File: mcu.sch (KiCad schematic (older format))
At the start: 13 parts, among them J3 jtag conector, U4 STM32F103C8Tx, U5 STM32F031K6Ux

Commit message: duży update, gotowe pcb
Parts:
- removed R16: 10R, Resistor_SMD:R_0603_1608Metric, symbol Device:R
- removed U5: STM32F031K6Ux, Package_DFN_QFN:QFN-32-1EP_5x5mm_P0.5mm_EP3.45x3.45mm, symbol MCU_ST_STM32F0:STM32F031K6Ux
- added C20: 100n, Capacitor_SMD:C_0603_1608Metric_Pad1.05x0.95mm_HandSolder, symbol Device:C
- added J4: Conn_01x04_Female, Connector_PinHeader_2.54mm:PinHeader_1x04_P2.54mm_Vertical, symbol Connector:Conn_01x04_Female
- R14: footprint (none) -> Resistor_SMD:R_0603_1608Metric_Pad1.05x0.95mm_HandSolder
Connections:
- net labels added: scl, sda
- wire segments 78 -> 69
- no-connect marks 0 -> 28
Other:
- note removed: "STM32F030C8Tx pasuje wystrczy zrobć nc na 36 i 35 \nfootprint się zgadza tylko \npin 36 to VDD\npin35 to GND\n\n"

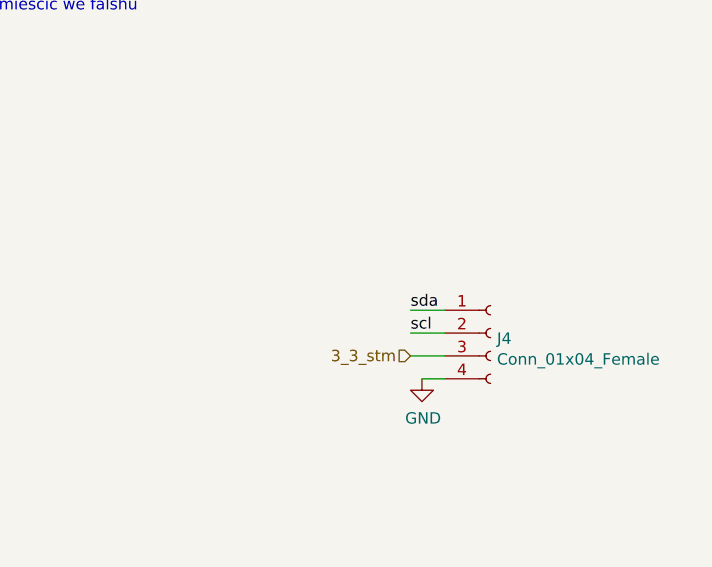
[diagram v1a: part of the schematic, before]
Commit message: dodanie pullup do i2c i screenow
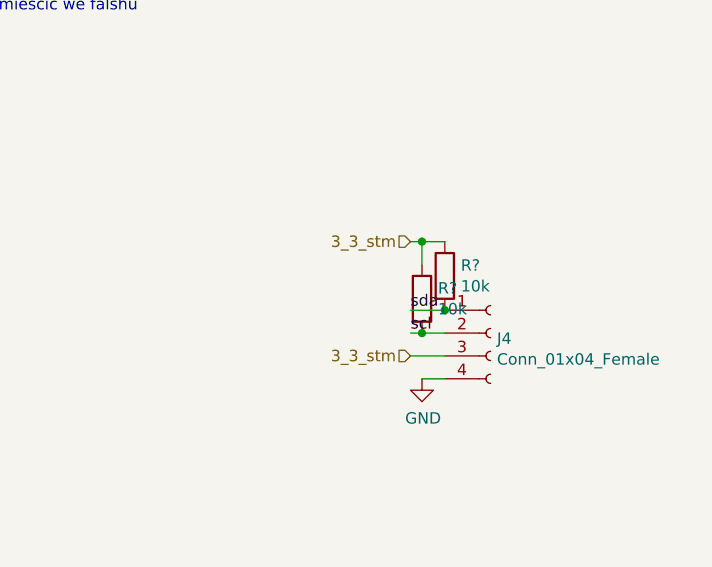
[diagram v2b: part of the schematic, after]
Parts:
- added R? (x2): 10k, Resistor_SMD:R_0603_1608Metric, symbol Device:R
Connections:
- wire segments 69 -> 73
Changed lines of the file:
@@
 	8050 3500 8200 3500
 Wire Wire Line
-	8200 3400 8050 3400
+	8200 3400 8100 3400
 Wire Wire Line
 	8200 3300 8050 3300
@@
 Wire Wire Line
 	4700 1700 4700 1600
+$Comp
+L Device:R R?
+U 1 1 5CEC68D2
+P 8200 3150
+F 0 "R?" H 8270 3196 50  0000 L CNN
+F 1 "10k" H 8270 3105 50  0000 L CNN
+F 2 "Resistor_SMD:R_0603_1608Metric" V 8130 3150 50  0001 C CNN
+F 3 "~" H 8200 3150 50  0001 C CNN
+	1    8200 3150
+	1    0    0    -1
+$EndComp
+Connection ~ 8200 3300
+$Comp
+L Device:R R?
+U 1 1 5CEC6FCF
+P 8100 3250
+F 0 "R?" H 8170 3296 50  0000 L CNN
+F 1 "10k" H 8170 3205 50  0000 L CNN
+F 2 "Resistor_SMD:R_0603_1608Metric" V 8030 3250 50  0001 C CNN
+F 3 "~" H 8100 3250 50  0001 C CNN
+	1    8100 3250
+	1    0    0    -1
+$EndComp
+Connection ~ 8100 3400
+Wire Wire Line
+	8100 3400 8050 3400
+Text HLabel 8050 3000 0    50   Input ~ 0
+3_3_stm
+Wire Wire Line
+	8050 3000 8100 3000
+Wire Wire Line
+	8100 3000 8100 3100
+Wire Wire Line
+	8100 3000 8200 3000
+Connection ~ 8100 3000
 $EndSCHEMATC

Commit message: poprawki na sch
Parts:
- removed J3: jtag conector, Connector_PinHeader_1.27mm:PinHeader_2x04_P1.27mm_Vertical_SMD, symbol Connector_Generic_MountingPin:Conn_01x10_MountingPin
- added J3: Conn_02x04_Odd_Even, Connector_PinHeader_1.27mm:PinHeader_2x04_P1.27mm_Vertical_SMD, symbol Connector_Generic:Conn_02x04_Odd_Even
- gave numbers to parts that had none: 2
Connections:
- wire segments 73 -> 76
- no-connect marks 28 -> 25
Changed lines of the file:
@@
 EESchema Schematic File Version 4
 LIBS:WELLER-cache
-EELAYER 29 0
+EELAYER 26 0
 EELAYER END
 $Descr A4 11693 8268
@@
 Wire Wire Line
 	2500 2250 2500 2650
-$Comp
-L Connector_Generic_MountingPin:Conn_01x10_MountingPin J3
-U 1 1 5CB74020
-P 2250 4800
-F 0 "J3" H 2337 4622 50  0000 L CNN
-F 1 "jtag conector" H 2337 4713 50  0000 L CNN
-F 2 "Connector_PinHeader_1.27mm:PinHeader_2x04_P1.27mm_Vertical_SMD" H 2250 4800 50  0001 C CNN
-F 3 "~" H 2250 4800 50  0001 C CNN
-	1    2250 4800
-	-1   0    0    1
-$EndComp
 Text Notes 5700 2000 0    50   ~ 0
 można by dodać eeprom do zapisaywania danych dot temp ?\n->powinno się zmieścić we falshu\n
@@
 Wire Wire Line
 	4400 5900 4500 5900
-Text Label 2650 4300 0    50   ~ 0
+Text Label 1600 4200 0    50   ~ 0
 nRST
-Wire Wire Line
-	2450 4300 2650 4300
-Wire Wire Line
-	2450 5100 2800 5100
-Wire Wire Line
-	2450 4900 2800 4900
-Text Label 2800 5100 0    50   ~ 0
+Text Label 1600 4400 0    50   ~ 0
 SWDIO
-Text Label 2800 4900 0    50   ~ 0
+Text Label 1600 4300 0    50   ~ 0
 SWCLK
 Connection ~ 4800 2350
 Wire Wire Line
 	4800 2350 4800 2500
-Text Label 2800 5200 0    50   ~ 0
+Text Label 1600 4500 0    50   ~ 0
 3_3v
-Wire Wire Line
-	2800 5200 2450 5200
-$Comp
-L power:GND #PWR0132
-U 1 1 5CC8470F
-P 2600 5000
-F 0 "#PWR0132" H 2600 4750 50  0001 C CNN
-F 1 "GND" H 2605 4827 50  0000 C CNN
-F 2 "" H 2600 5000 50  0001 C CNN
-F 3 "" H 2600 5000 50  0001 C CNN
-	1    2600 5000
-	0    -1   -1   0
-$EndComp
-Wire Wire Line
-	2600 5000 2450 5000
-$Comp
-L power:GND #PWR0133
-U 1 1 5CC87D51
-P 2600 4800
-F 0 "#PWR0133" H 2600 4550 50  0001 C CNN
-F 1 "GND" H 2605 4627 50  0000 C CNN
-F 2 "" H 2600 4800 50  0001 C CNN
-F 3 "" H 2600 4800 50  0001 C CNN
-	1    2600 4800
-	0    -1   -1   0
-$EndComp
-Wire Wire Line
-	2600 4800 2450 4800
 $Comp
 L power:GND #PWR0134
 U 1 1 5CC89512
-P 2600 4600
-F 0 "#PWR0134" H 2600 4350 50  0001 C CNN
-F 1 "GND" H 2605 4427 50  0000 C CNN
-F 2 "" H 2600 4600 50  0001 C CNN
-F 3 "" H 2600 4600 50  0001 C CNN
-	1    2600 4600
-	0    -1   -1   0
-$EndComp
-Wire Wire Line
-	2600 4600 2450 4600
-$Comp
-L power:GND #PWR0135
-U 1 1 5CC8BC59
-P 2600 4400
-F 0 "#PWR0135" H 2600 4150 50  0001 C CNN
-F 1 "GND" H 2605 4227 50  0000 C CNN
-F 2 "" H 2600 4400 50  0001 C CNN
-F 3 "" H 2600 4400 50  0001 C CNN
-	1    2600 4400
-	0    -1   -1   0
-$EndComp
-Wire Wire Line
-	2600 4400 2450 4400
+P 900 4300
+F 0 "#PWR0134" H 900 4050 50  0001 C CNN
+F 1 "GND" H 905 4127 50  0000 C CNN
+F 2 "" H 900 4300 50  0001 C CNN
+F 3 "" H 900 4300 50  0001 C CNN
+	1    900  4300
+	0    1    1    0
+$EndComp
 Wire Wire Line
 	4600 2050 4600 2600
@@
 NoConn ~ 3900 5300
 NoConn ~ 3900 5400
-NoConn ~ 2450 4500
-NoConn ~ 2450 4700
-NoConn ~ 2250 4100
 $Comp
 L power:PWR_FLAG #FLG0101
@@
 	4700 1700 4700 1600
 $Comp
-L Device:R R?
+L Device:R R17
 U 1 1 5CEC68D2
 P 8200 3150
-F 0 "R?" H 8270 3196 50  0000 L CNN
+F 0 "R17" H 8270 3196 50  0000 L CNN
 F 1 "10k" H 8270 3105 50  0000 L CNN
 F 2 "Resistor_SMD:R_0603_1608Metric" V 8130 3150 50  0001 C CNN
@@
 Connection ~ 8200 3300
 $Comp
-L Device:R R?
+L Device:R R16
 U 1 1 5CEC6FCF
 P 8100 3250
-F 0 "R?" H 8170 3296 50  0000 L CNN
+F 0 "R16" H 8170 3296 50  0000 L CNN
 F 1 "10k" H 8170 3205 50  0000 L CNN
 F 2 "Resistor_SMD:R_0603_1608Metric" V 8030 3250 50  0001 C CNN
@@
 	8100 3000 8200 3000
 Connection ~ 8100 3000
+$Comp
+L Connector_Generic:Conn_02x04_Odd_Even J3
+U 1 1 5CEE64F6
+P 1200 4300
+F 0 "J3" H 1250 4617 50  0000 C CNN
+F 1 "Conn_02x04_Odd_Even" H 1250 4526 50  0000 C CNN
+F 2 "Connector_PinHeader_1.27mm:PinHeader_2x04_P1.27mm_Vertical_SMD" H 1200 4300 50  0001 C CNN
+F 3 "~" H 1200 4300 50  0001 C CNN
+	1    1200 4300
+	1    0    0    -1
+$EndComp
+Wire Wire Line
+	1000 4200 900  4200
+Wire Wire Line
+	900  4200 900  4300
+Wire Wire Line
+	900  4300 900  4400
+Wire Wire Line
+	900  4500 1000 4500
+Connection ~ 900  4300
+Wire Wire Line
+	1000 4400 900  4400
+Connection ~ 900  4400
+Wire Wire Line
+	900  4400 900  4500
+Wire Wire Line
+	900  4300 1000 4300
+Wire Wire Line
+	1500 4200 1600 4200
+Wire Wire Line
+	1600 4300 1500 4300
+Wire Wire Line
+	1500 4400 1600 4400
+Wire Wire Line
+	1600 4500 1500 4500
 $EndSCHEMATC

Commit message: duży update, drc przechodzi
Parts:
- added R18: 560k, Resistor_SMD:R_0603_1608Metric, symbol Device:R
- added R19: 100k, Resistor_SMD:R_0603_1608Metric, symbol Device:R
- added U5: SM353LT, Package_TO_SOT_SMD:SOT-23, symbol Sensor_Magnetic:SM353LT
- J3: value Conn_02x04_Odd_Even -> debug+programing; footprint Connector_PinHeader_1.27mm:PinHeader_2x04_P1.27mm_Vertical_SMD -> Connector_PinHeader_1.27mm:PinHeader_2x05_P1.27mm_Vertical_SMD; symbol Connector_Generic:Conn_02x04_Odd_Even -> Connector_Generic:Conn_02x05_Odd_Even
- J4: value Conn_01x04_Female -> I2c oled
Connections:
- net labels added: 12V, hall_in, input_divider, usart_ck, usart_rx, usart_tx
- net labels removed: 3_3v
- wire segments 76 -> 88
- no-connect marks 25 -> 23
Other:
- note added: "3V <- 20V\n"
- moved on the sheet: C12, C13, C14, C15, C16, C17, C20, J4, R13, R14, R15, R16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

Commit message: dodanie pomiaru napięcia zasilającego grzałkę
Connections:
- net input_sense: now reaches U4.14 (PA4)
- no-connect marks 23 -> 21
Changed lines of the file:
@@
 Wire Wire Line
 	5750 4100 6000 4100
-NoConn ~ 7300 3900
 NoConn ~ 7300 4000
 NoConn ~ 7300 4100
@@
 	2450 1600 2450 7300
 NoConn ~ 6000 2800
-NoConn ~ 5700 2900
 Wire Wire Line
 	6900 1950 6900 2200
+Wire Wire Line
+	7400 3900 7300 3900
+Text HLabel 7400 3900 2    50   Input ~ 0
+input_sense
 $EndSCHEMATC

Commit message: poprawki głownie na pcb zaokrąglenie strony z grotem
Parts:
- removed R18: 560k, Resistor_SMD:R_0603_1608Metric, symbol Device:R
- removed R19: 100k, Resistor_SMD:R_0603_1608Metric, symbol Device:R
- added C25: 100n, Capacitor_SMD:C_0603_1608Metric_Pad1.05x0.95mm_HandSolder, symbol Device:C
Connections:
- net input_divider is gone; now on net input_sense: U4.11 (PA1)
- net 3_3_stm: now also C25.2
- net GND: now also C25.1
- net input_sense: no longer U4.14 (PA4)
- no-connect marks 21 -> 22
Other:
- note removed: "3V <- 20V\n"
- note removed: "można by dodać eeprom do zapisaywania danych dot temp ?\n->powinno się zmieścić we falshu\n"
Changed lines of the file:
@@
 Wire Wire Line
 	4600 1850 4600 2250
-Text Notes 7800 1600 0    50   ~ 0
-można by dodać eeprom do zapisaywania danych dot temp ?\n->powinno się zmieścić we falshu\n
 Text HLabel 5850 3100 0    50   BiDi ~ 0
 sw1
@@
 Wire Wire Line
 	1900 6850 1800 6850
-Text Label 7850 3600 2    50   ~ 0
-input_divider
 Wire Wire Line
 	7400 3800 7300 3800
@@
 	1800 5600 1800 5500
 Wire Wire Line
-	1800 4900 1800 4800
+	1800 4900 1800 4850
 Text HLabel 1800 4800 1    50   Input ~ 0
 3_3_stm
@@
 Wire Notes Line
 	700  4350 2450 4350
-Text HLabel 2150 3150 2    50   Input ~ 0
-12V
-$Comp
-L Device:R R18
-U 1 1 5CF9661D
-P 1750 3350
-F 0 "R18" H 1820 3396 50  0000 L CNN
-F 1 "560k" H 1820 3305 50  0000 L CNN
-F 2 "Resistor_SMD:R_0603_1608Metric" V 1680 3350 50  0001 C CNN
-F 3 "~" H 1750 3350 50  0001 C CNN
-	1    1750 3350
-	-1   0    0    -1
-$EndComp
-$Comp
-L Device:R R19
-U 1 1 5CF96623
-P 1750 3800
-F 0 "R19" H 1820 3846 50  0000 L CNN
-F 1 "100k" H 1820 3755 50  0000 L CNN
-F 2 "Resistor_SMD:R_0603_1608Metric" V 1680 3800 50  0001 C CNN
-F 3 "~" H 1750 3800 50  0001 C CNN
-	1    1750 3800
-	-1   0    0    -1
-$EndComp
-Wire Wire Line
-	2150 3150 1750 3150
-Wire Wire Line
-	1750 3150 1750 3200
-$Comp
-L power:GND #PWR02
-U 1 1 5CF9662B
-P 1750 4050
-F 0 "#PWR02" H 1750 3800 50  0001 C CNN
-F 1 "GND" H 1755 3877 50  0000 C CNN
-F 2 "" H 1750 4050 50  0001 C CNN
-F 3 "" H 1750 4050 50  0001 C CNN
-	1    1750 4050
-	-1   0    0    -1
-$EndComp
-Wire Wire Line
-	1750 3950 1750 4050
-Wire Wire Line
-	1750 3500 1750 3600
-Text Label 850  3600 0    50   ~ 0
-input_divider
-Connection ~ 1750 3600
-Wire Wire Line
-	1750 3600 1750 3650
-Wire Wire Line
-	850  3600 1750 3600
-Text Notes 1950 3150 3    50   ~ 0
- 3V  <- 20V\n
-Wire Notes Line
-	1750 3600 1900 3600
-Wire Notes Line
-	1900 3250 1850 3250
-Wire Notes Line
-	1850 3250 1850 3150
-Wire Wire Line
-	7300 3600 7850 3600
 Wire Notes Line
 	2450 3050 700  3050
@@
 Wire Wire Line
 	6900 1950 6900 2200
-Wire Wire Line
-	7400 3900 7300 3900
-Text HLabel 7400 3900 2    50   Input ~ 0
+$Comp
+L Device:C C25
+U 1 1 5D126A2E
+P 1950 4850
+F 0 "C25" V 1698 4850 50  0000 C CNN
+F 1 "100n" V 1789 4850 50  0000 C CNN
+F 2 "Capacitor_SMD:C_0603_1608Metric_Pad1.05x0.95mm_HandSolder" H 1988 4700 50  0001 C CNN
+F 3 "~" H 1950 4850 50  0001 C CNN
+	1    1950 4850
+	0    1    1    0
+$EndComp
+Connection ~ 1800 4850
+Wire Wire Line
+	1800 4850 1800 4800
+$Comp
+L power:GND #PWR0142
+U 1 1 5D12749D
+P 2100 4850
+F 0 "#PWR0142" H 2100 4600 50  0001 C CNN
+F 1 "GND" H 2105 4677 50  0000 C CNN
+F 2 "" H 2100 4850 50  0001 C CNN
+F 3 "" H 2100 4850 50  0001 C CNN
+	1    2100 4850
+	0    -1   -1   0
+$EndComp
+Wire Wire Line
+	7400 3600 7300 3600
+Text HLabel 7400 3600 2    50   Input ~ 0
 input_sense
+NoConn ~ 7300 3900
 $EndSCHEMATC

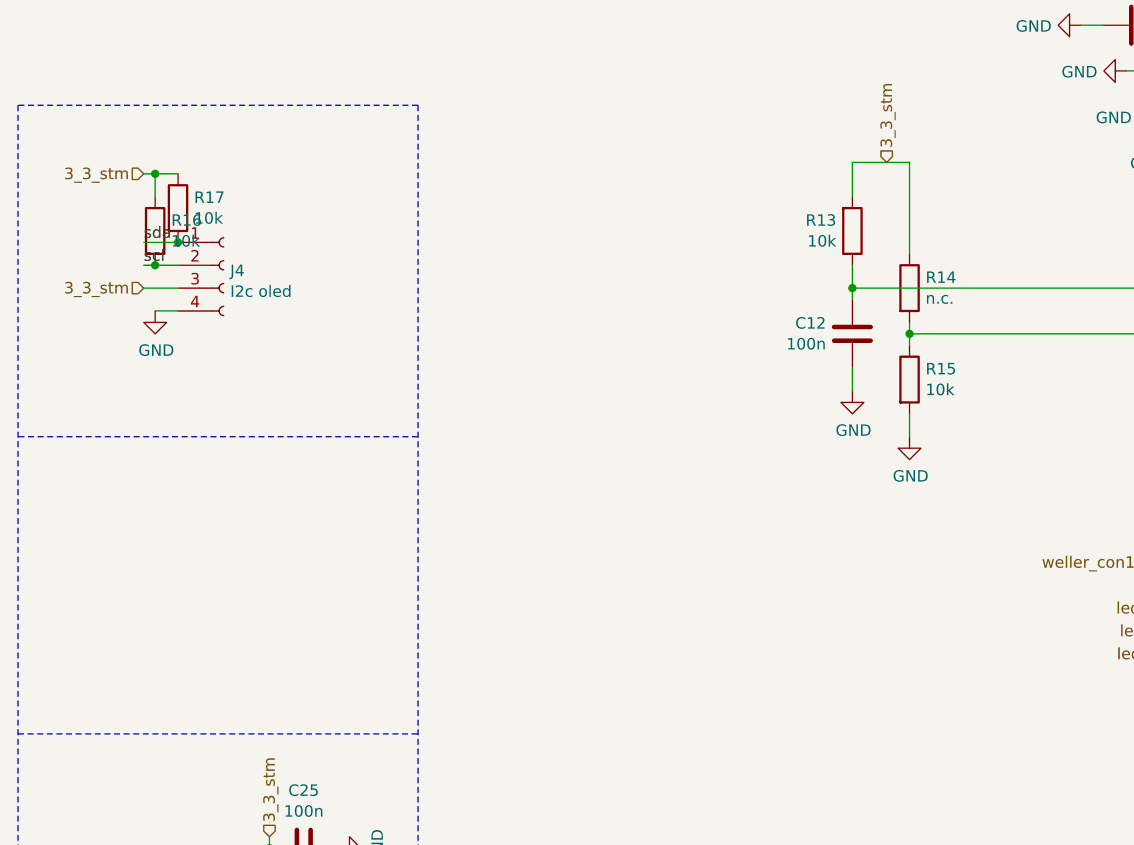
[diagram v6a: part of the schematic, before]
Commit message: wyciecie przy gnieździe jack - dodanie 3d gniazda, update jpg
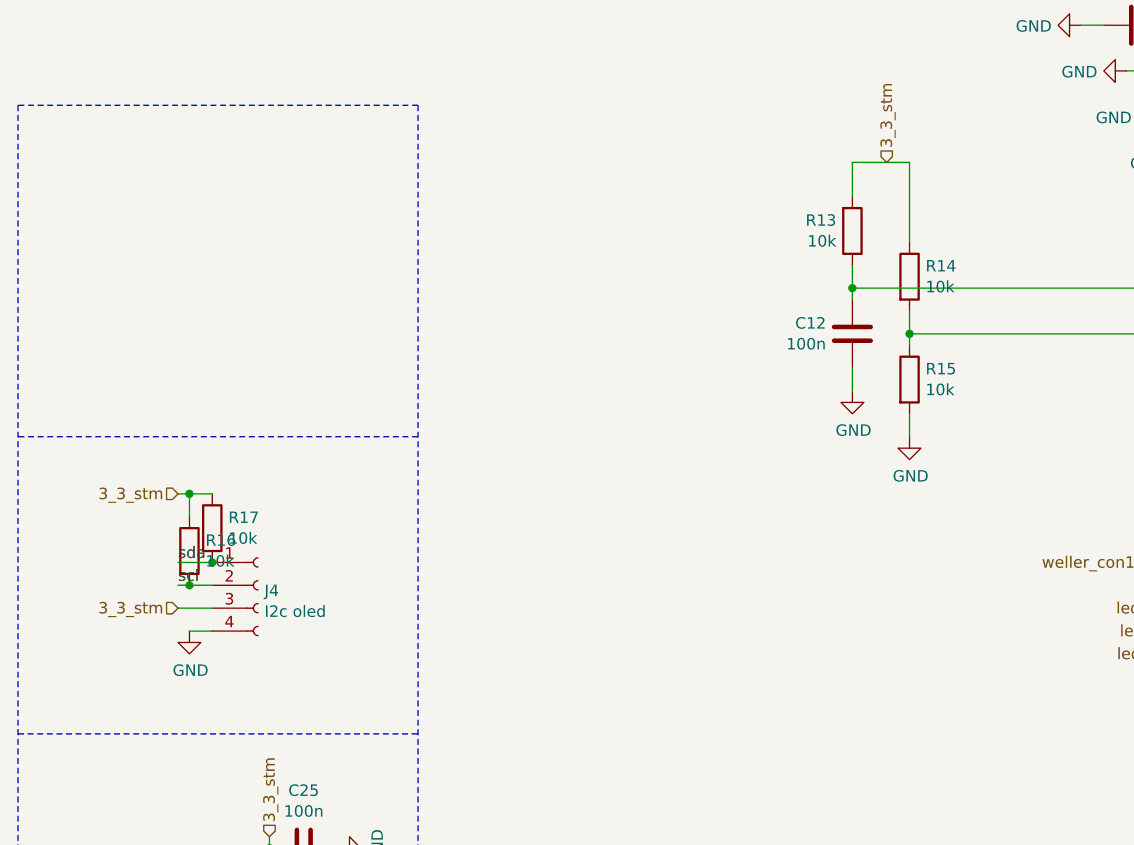
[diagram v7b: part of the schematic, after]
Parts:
- R14: value n.c. -> 10k; footprint Resistor_SMD:R_0603_1608Metric_Pad1.05x0.95mm_HandSolder -> Resistor_SMD:R_0603_1608Metric
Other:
- moved on the sheet: J4, R16, R17
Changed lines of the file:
@@
 	6800 5500 6800 5200
-$Comp
-L Device:R R14
-U 1 1 5CB55440
-P 4600 2400
-F 0 "R14" H 4670 2446 50  0000 L CNN
-F 1 "n.c." H 4670 2355 50  0000 L CNN
-F 2 "Resistor_SMD:R_0603_1608Metric_Pad1.05x0.95mm_HandSolder" V 4530 2400 50  0001 C CNN
-F 3 "~" H 4600 2400 50  0001 C CNN
-	1    4600 2400
-	1    0    0    -1
-$EndComp
 $Comp
 L Device:R R15
@@
 	4350 2850 4350 2750
 Wire Wire Line
-	4600 2550 4600 2600
+	4600 2500 4600 2600
 Connection ~ 4600 2600
 Wire Wire Line
@@
 Wire Wire Line
 	4350 1850 4350 2000
-Wire Wire Line
-	4600 1850 4600 2250
 Text HLabel 5850 3100 0    50   BiDi ~ 0
 sw1
@@
 L Connector:Conn_01x04_Female J4
 U 1 1 5CEC6946
-P 1600 2300
-F 0 "J4" H 1628 2276 50  0000 L CNN
-F 1 "I2c oled " H 1628 2185 50  0000 L CNN
-F 2 "Connector_PinHeader_2.54mm:PinHeader_1x04_P2.54mm_Vertical" H 1600 2300 50  0001 C CNN
-F 3 "~" H 1600 2300 50  0001 C CNN
-	1    1600 2300
+P 1750 3700
+F 0 "J4" H 1778 3676 50  0000 L CNN
+F 1 "I2c oled " H 1778 3585 50  0000 L CNN
+F 2 "Connector_PinHeader_2.54mm:PinHeader_1x04_P2.54mm_Vertical" H 1750 3700 50  0001 C CNN
+F 3 "~" H 1750 3700 50  0001 C CNN
+	1    1750 3700
 	1    0    0    -1
 $EndComp
@@
 L power:GND #PWR0139
 U 1 1 5CEC799A
-P 1300 2500
-F 0 "#PWR0139" H 1300 2250 50  0001 C CNN
-F 1 "GND" H 1305 2327 50  0000 C CNN
-F 2 "" H 1300 2500 50  0001 C CNN
-F 3 "" H 1300 2500 50  0001 C CNN
-	1    1300 2500
-	1    0    0    -1
-$EndComp
-Wire Wire Line
-	1400 2500 1300 2500
-Text HLabel 1250 2400 0    50   Input ~ 0
+P 1450 3900
+F 0 "#PWR0139" H 1450 3650 50  0001 C CNN
+F 1 "GND" H 1455 3727 50  0000 C CNN
+F 2 "" H 1450 3900 50  0001 C CNN
+F 3 "" H 1450 3900 50  0001 C CNN
+	1    1450 3900
+	1    0    0    -1
+$EndComp
+Wire Wire Line
+	1550 3900 1450 3900
+Text HLabel 1400 3800 0    50   Input ~ 0
 3_3_stm
 Wire Wire Line
-	1250 2400 1400 2400
-Wire Wire Line
-	1400 2300 1300 2300
-Wire Wire Line
-	1400 2200 1250 2200
-Text Label 1250 2200 0    50   ~ 0
+	1400 3800 1550 3800
+Wire Wire Line
+	1550 3700 1450 3700
+Wire Wire Line
+	1550 3600 1400 3600
+Text Label 1400 3600 0    50   ~ 0
 sda
-Text Label 1250 2300 0    50   ~ 0
+Text Label 1400 3700 0    50   ~ 0
 scl
 Text Label 5750 4200 0    50   ~ 0
@@
 L Device:R R17
 U 1 1 5CEC68D2
-P 1400 2050
-F 0 "R17" H 1470 2096 50  0000 L CNN
-F 1 "10k" H 1470 2005 50  0000 L CNN
-F 2 "Resistor_SMD:R_0603_1608Metric" V 1330 2050 50  0001 C CNN
-F 3 "~" H 1400 2050 50  0001 C CNN
-	1    1400 2050
-	1    0    0    -1
-$EndComp
-Connection ~ 1400 2200
+P 1550 3450
+F 0 "R17" H 1620 3496 50  0000 L CNN
+F 1 "10k" H 1620 3405 50  0000 L CNN
+F 2 "Resistor_SMD:R_0603_1608Metric" V 1480 3450 50  0001 C CNN
+F 3 "~" H 1550 3450 50  0001 C CNN
+	1    1550 3450
+	1    0    0    -1
+$EndComp
+Connection ~ 1550 3600
 $Comp
 L Device:R R16
 U 1 1 5CEC6FCF
-P 1300 2150
-F 0 "R16" H 1370 2196 50  0000 L CNN
-F 1 "10k" H 1370 2105 50  0000 L CNN
-F 2 "Resistor_SMD:R_0603_1608Metric" V 1230 2150 50  0001 C CNN
-F 3 "~" H 1300 2150 50  0001 C CNN
-	1    1300 2150
-	1    0    0    -1
-$EndComp
-Connection ~ 1300 2300
-Wire Wire Line
-	1300 2300 1250 2300
-Text HLabel 1250 1900 0    50   Input ~ 0
+P 1450 3550
+F 0 "R16" H 1520 3596 50  0000 L CNN
+F 1 "10k" H 1520 3505 50  0000 L CNN
+F 2 "Resistor_SMD:R_0603_1608Metric" V 1380 3550 50  0001 C CNN
+F 3 "~" H 1450 3550 50  0001 C CNN
+	1    1450 3550
+	1    0    0    -1
+$EndComp
+Connection ~ 1450 3700
+Wire Wire Line
+	1450 3700 1400 3700
+Text HLabel 1400 3300 0    50   Input ~ 0
 3_3_stm
 Wire Wire Line
-	1250 1900 1300 1900
-Wire Wire Line
-	1300 1900 1300 2000
-Wire Wire Line
-	1300 1900 1400 1900
-Connection ~ 1300 1900
+	1400 3300 1450 3300
+Wire Wire Line
+	1450 3300 1450 3400
+Wire Wire Line
+	1450 3300 1550 3300
+Connection ~ 1450 3300
 $Comp
 L Connector_Generic:Conn_02x05_Odd_Even J3
@@
 input_sense
 NoConn ~ 7300 3900
+Wire Wire Line
+	4600 1850 4600 2200
+$Comp
+L Device:R R14
+U 1 1 5D126D6E
+P 4600 2350
+F 0 "R14" H 4670 2396 50  0000 L CNN
+F 1 "10k" H 4670 2305 50  0000 L CNN
+F 2 "Resistor_SMD:R_0603_1608Metric" V 4530 2350 50  0001 C CNN
+F 3 "~" H 4600 2350 50  0001 C CNN
+	1    4600 2350
+	1    0    0    -1
+$EndComp
 $EndSCHEMATC
